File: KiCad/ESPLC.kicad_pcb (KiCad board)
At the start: 2 copper layers, 98.5 x 94 mm, 51 parts, among them J1 D1, J10 A2, J11 USB_C_Receptacle_USB2.0_16P, J2 D2, J3 D3, J4 D4, J5 Screw_Terminal_01x03, J6 Screw_Terminal_01x03, J7 Screw_Terminal_01x03, J8 Screw_Terminal_01x03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

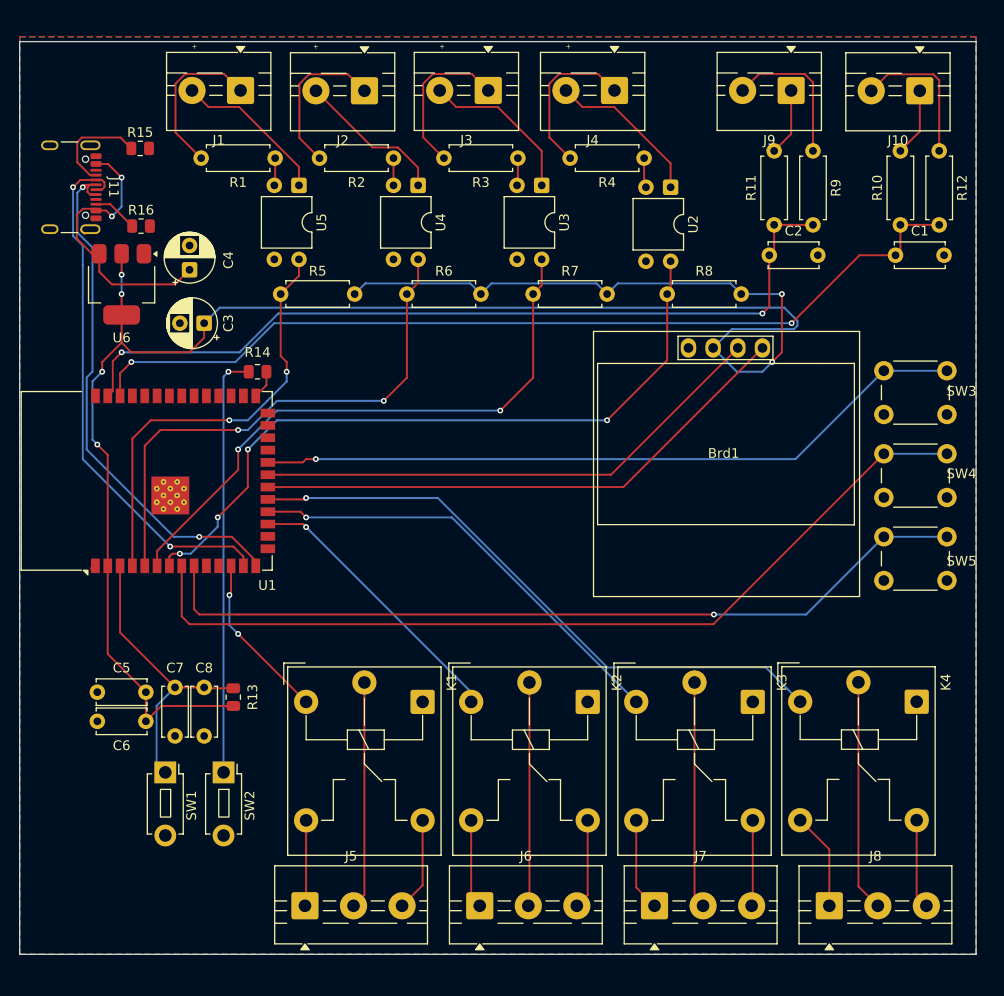
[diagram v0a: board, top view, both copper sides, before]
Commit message: Added Software section to README, updated Gerber
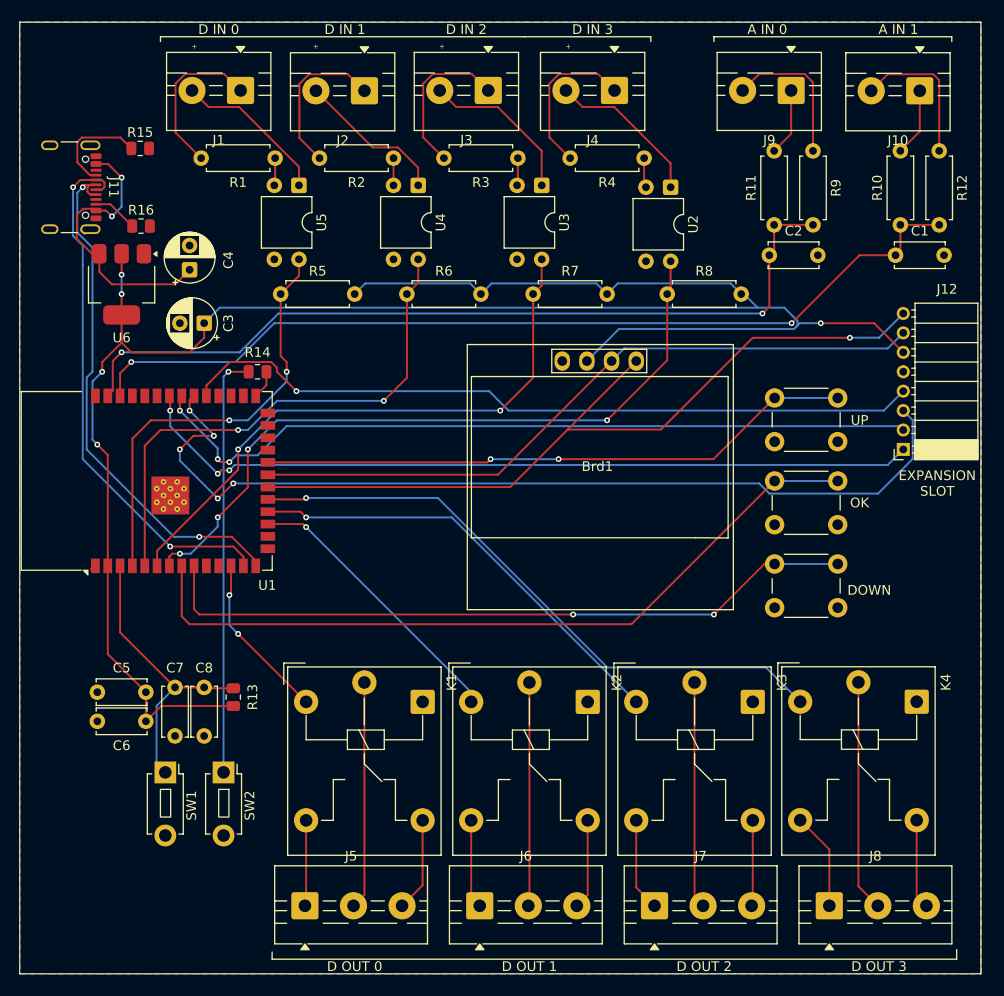
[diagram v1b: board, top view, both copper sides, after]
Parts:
- added J12: Conn_01x08_Socket, Connector_PinSocket_2.00mm:PinSocket_1x08_P2.00mm_Horizontal, F.Cu at (177.5, 79.0)
- moved Brd1 13.1 mm to (146.0, 80.5)
- moved DOWN 11.6 mm to (164.2, 90.8)
- moved OK 11.6 mm to (164.2, 82.2)
- moved UP 11.6 mm to (164.2, 73.7)
- renumbered SW5 to DOWN, SW4 to OK, SW3 to UP
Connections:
- U1 pad 31: unconnected-(U1-IO38-Pad31) -> GPIO1
- U1 pad 32: unconnected-(U1-IO39-Pad32) -> GPIO2
- U1 pad 33: unconnected-(U1-IO40-Pad33) -> GPIO3
- U1 pad 34: unconnected-(U1-IO41-Pad34) -> GPIO4
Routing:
- net GPIO2: track 0.00 -> 95.6 mm, vias 0 -> 5
- net GPIO4: track 0.00 -> 81.7 mm, vias 0 -> 3
- net GPIO3: track 0.00 -> 80.6 mm, vias 0 -> 3
- net GPIO1: track 0.00 -> 77.0 mm, vias 0 -> 1
- net SDA: track 56.9 -> 82.8 mm, vias 0 -> 1
- net SCL: track 53.8 -> 71.5 mm
- net UP: track 73.8 -> 61.4 mm, vias 1 -> 2
- net OK: track 91.6 -> 79.2 mm
- net DOWN: track 85.5 -> 73.1 mm, vias 1 -> 2
- net +3V3: track 207.5 -> 216.7 mm, vias 6 -> 5
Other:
- board size 98.5 x 94 mm -> 99 x 98 mm
- board text added: "3V3"
- board text added: "A IN 0"
- board text added: "A IN 1"
- board text added: "D IN 0"
- board text added: "D IN 1"
- board text added: "D IN 2"
- board text added: "D IN 3"
- board text added: "D OUT 0"
- board text added: "D OUT 1"
- board text added: "D OUT 2"
- board text added: "D OUT 3"
- board text added: "EXPANSION SLOT"
- board text added: "GND"
- board text added: "GPIO1"
- board text added: "GPIO10"
- board text added: "GPIO11"
- board text added: "GPIO2"
- board text added: "GPIO3"
- board text added: "GPIO4"
- board text added: "GPIO5"
- board text added: "GPIO6"
- board text added: "GPIO7"
- board text added: "GPIO8"
- board text added: "GPIO9"
- board text added: "SCL"
- board text added: "SDA"
